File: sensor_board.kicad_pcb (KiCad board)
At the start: 2 copper layers, 96.5 x 64.8 mm, 13 parts, among them P1 CONN_01X06, P2 CONN_01X10

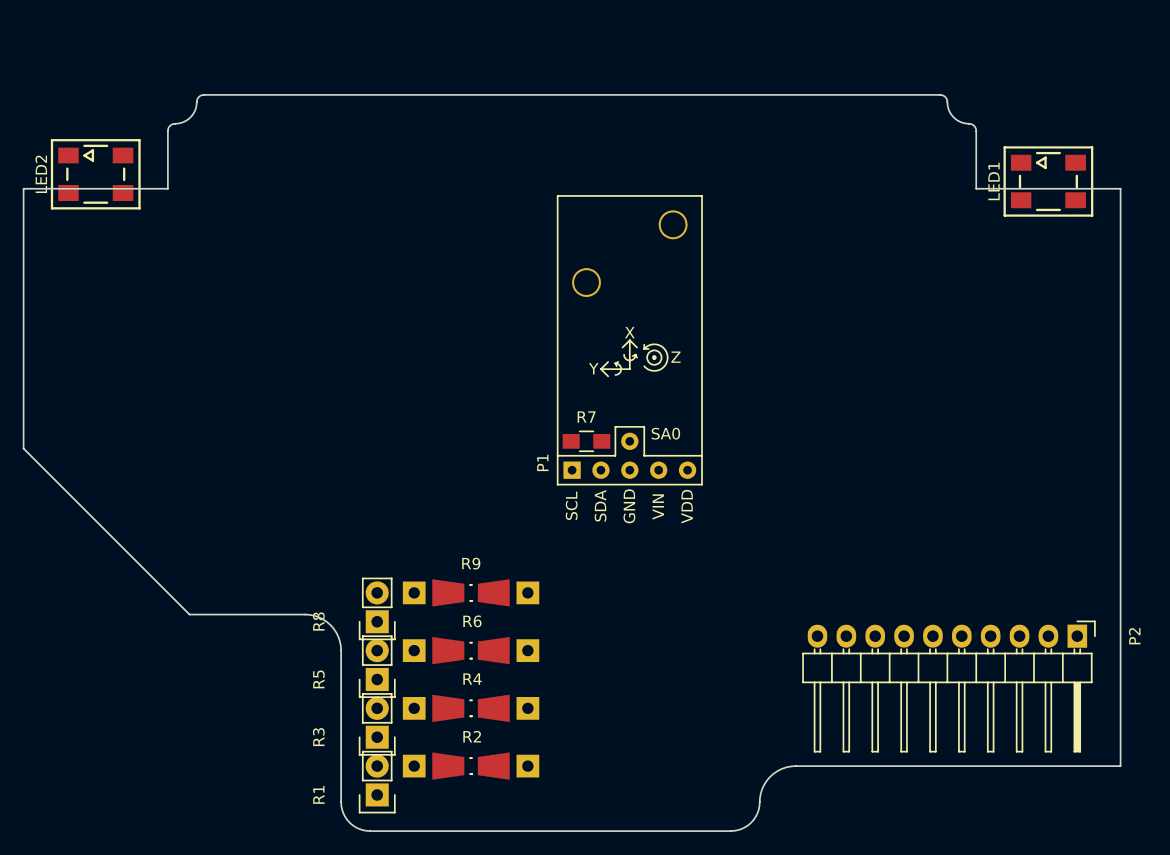
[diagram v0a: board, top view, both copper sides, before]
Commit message: Cleaned up schematics and sensor board PCB
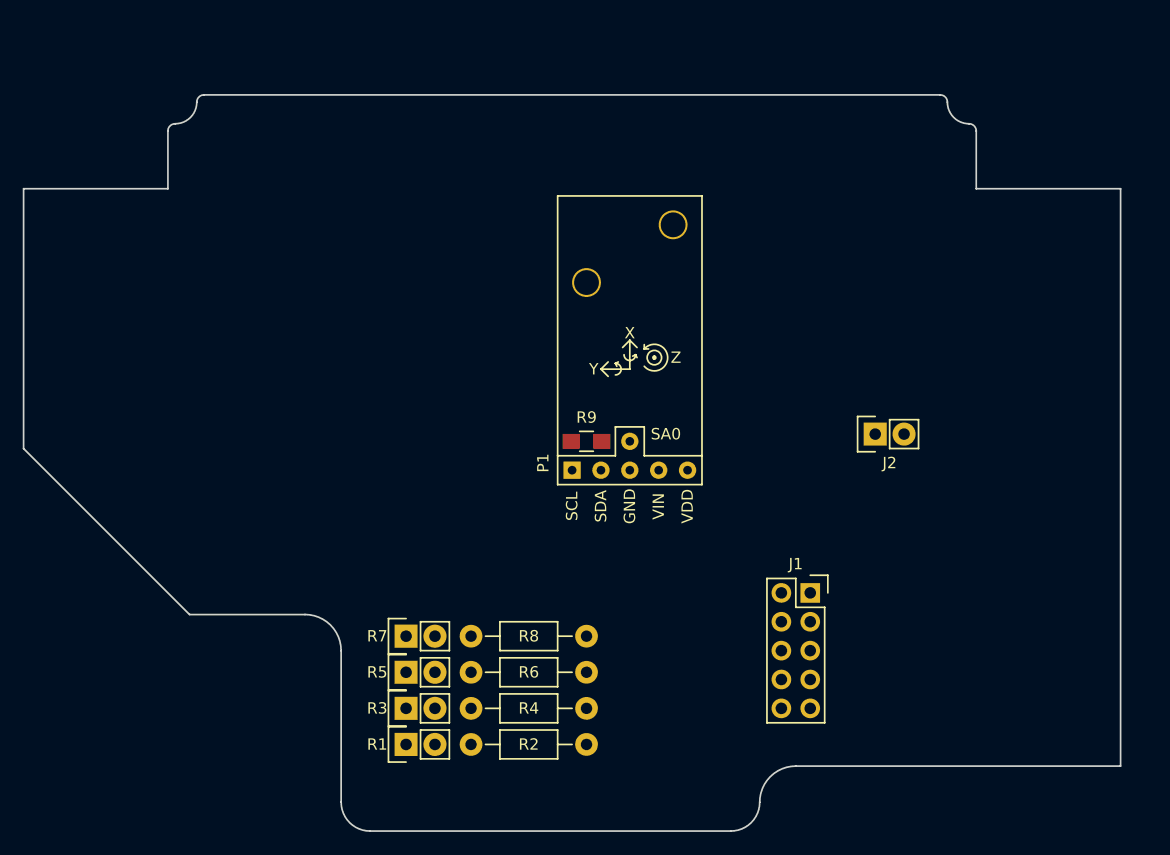
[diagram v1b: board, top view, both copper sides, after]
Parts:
- removed LED1, LED2: WS2812B, custom:PLCC4-5050
- removed P2: CONN_01X10, Pin_Headers:Pin_Header_Angled_1x10
- removed the R9 at (143.5, 123.8)
- added J1: HEADER_5x2, Socket_Strips:Socket_Strip_Straight_2x05, F.Cu at (173.4, 123.8)
- added J2: HEADER_2, Socket_Strips:Socket_Strip_Straight_1x02, F.Cu at (179.1, 109.9)
- added R8: 1M, Resistors_ThroughHole:Resistor_Horizontal_RM10mm, F.Cu at (143.5, 127.6)
- R2, R4, R6: value 100k -> 1M; footprint Resistors_Universal:Resistor_SMD+THTuniversal_0805to1206_RM10_HandSoldering_RevA_Date25Jun2010 -> Resistors_ThroughHole:Resistor_Horizontal_RM10mm
- moved R1 5.12 mm to (137.8, 137.2), turned to 0 degrees
- moved R3 3.59 mm to (137.8, 134.0), turned to 0 degrees
- moved R7 2.84 mm to (137.8, 127.6), turned to 0 degrees
- moved R5 2.62 mm to (137.8, 130.8), turned to 0 degrees
- moved R2 1.91 mm to (143.5, 137.2)
- moved R6 1.91 mm to (143.5, 130.8)
- renumbered R8 to R7, R7 to R9

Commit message: Sensor board revised fit within a 5cmX5cm square
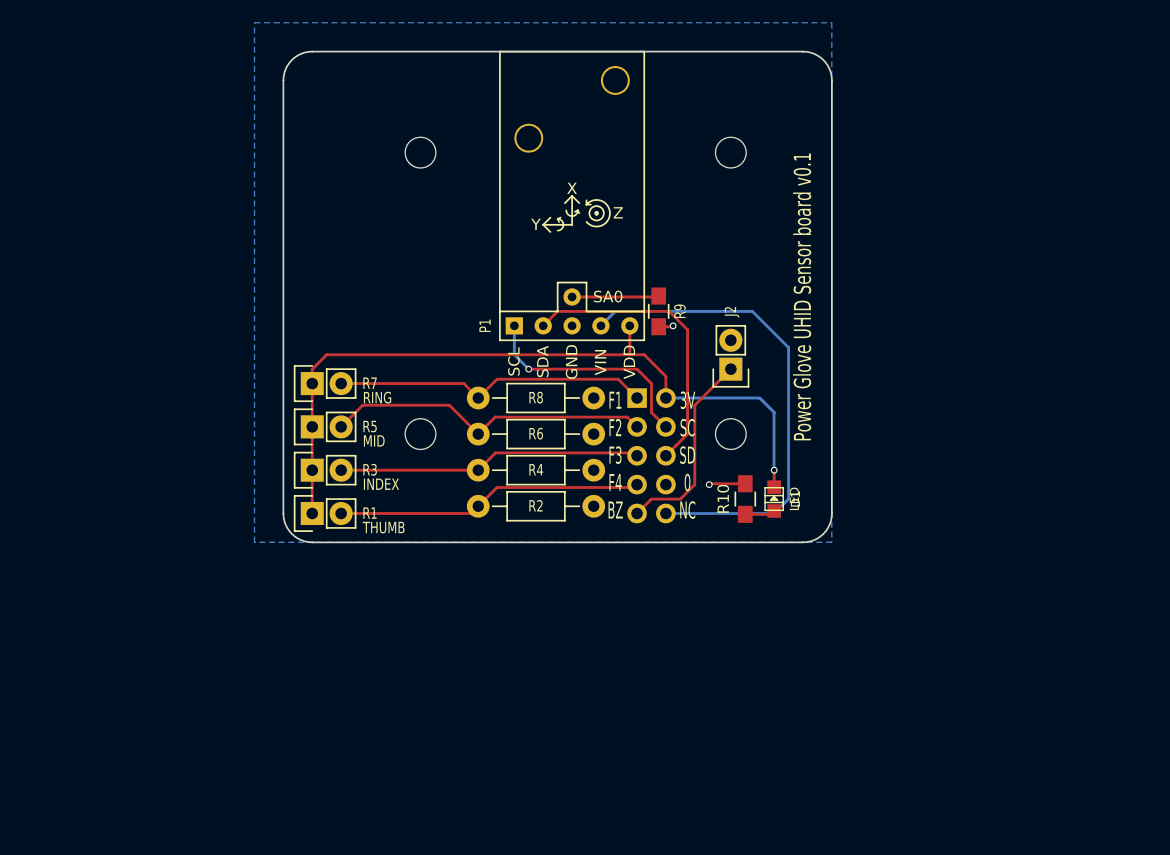
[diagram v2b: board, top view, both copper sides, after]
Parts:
- added D1: LED, w_smd_leds:Led_0805, F.Cu at (170.2, 115.6)
- added R10: 1k, Resistors_SMD:R_0805_HandSoldering, F.Cu at (167.6, 115.6)
- added REF**: MountingHole_2.7mm_M2.5, Mounting_Holes:MountingHole_2.7mm_M2.5, F.Cu at (139.1, 109.9)
- added REF**: MountingHole_2.7mm_M2.5, Mounting_Holes:MountingHole_2.7mm_M2.5, F.Cu at (166.4, 109.9)
- added REF**: MountingHole_2.7mm_M2.5, Mounting_Holes:MountingHole_2.7mm_M2.5, F.Cu at (166.4, 85.1)
- added REF**: MountingHole_2.7mm_M2.5, Mounting_Holes:MountingHole_2.7mm_M2.5, F.Cu at (139.1, 85.1)
- J1: moved to B.Cu
- moved R7 23.7 mm to (129.5, 105.4)
- moved R5 23.1 mm to (129.5, 109.2)
- moved J1 22.9 mm to (158.1, 106.7)
- moved R3 22.5 mm to (129.5, 113.0)
- moved R1 21.9 mm to (129.5, 116.8)
- moved R4 21.0 mm to (144.1, 113.0)
- moved R2 21.0 mm to (144.1, 116.2)
- moved R6 21.0 mm to (144.1, 109.9)
- moved R8 21.0 mm to (144.1, 106.7)
- moved J2 13.9 mm to (166.4, 104.1), turned to 90 degrees
- moved P1 13.7 mm to (152.4, 100.3)
- moved R9 13.1 mm to (160.0, 99.1), turned to 90 degrees
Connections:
- J1 pad 10: Net-(J1-Pad10) -> /VIN
- P1 pad 4: Net-(P1-Pad4) -> /VIN
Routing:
- net +3V3: track 0.00 -> 66.2 mm, vias 0 -> 1
- net /VIN: track 0.00 -> 43.0 mm
- net /FLEX_MIDDLE: track 0.00 -> 28.9 mm
- net /FLEX_RING: track 0.00 -> 27.9 mm
- net /FLEX_THUMB: track 0.00 -> 27.1 mm
- net /FLEX_INDEX: track 0.00 -> 26.8 mm
- net /IMU_SDA: track 0.00 -> 25.8 mm
- net /IMU_SCL: track 0.00 -> 20.0 mm, vias 0 -> 1
- net /BUZZER: track 0.00 -> 17.6 mm
- net Net-(P1-Pad6): track 0.00 -> 7.65 mm
- net GND: track 0.00 -> 4.51 mm, vias 0 -> 2
- net Net-(D1-Pad1): track 0.00 -> 2.66 mm
- added copper zone on B.Cu, net GND
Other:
- board size 96.5 x 64.8 mm -> 48.3 x 43.2 mm
- board text added: "3V SC SD 0 NC"
- board text added: "F1 F2 F3 F4 BZ"
- board text added: "INDEX"
- board text added: "MID"
- board text added: "Power Glove UHID Sensor board v0.1"
- board text added: "RING"
- board text added: "THUMB"

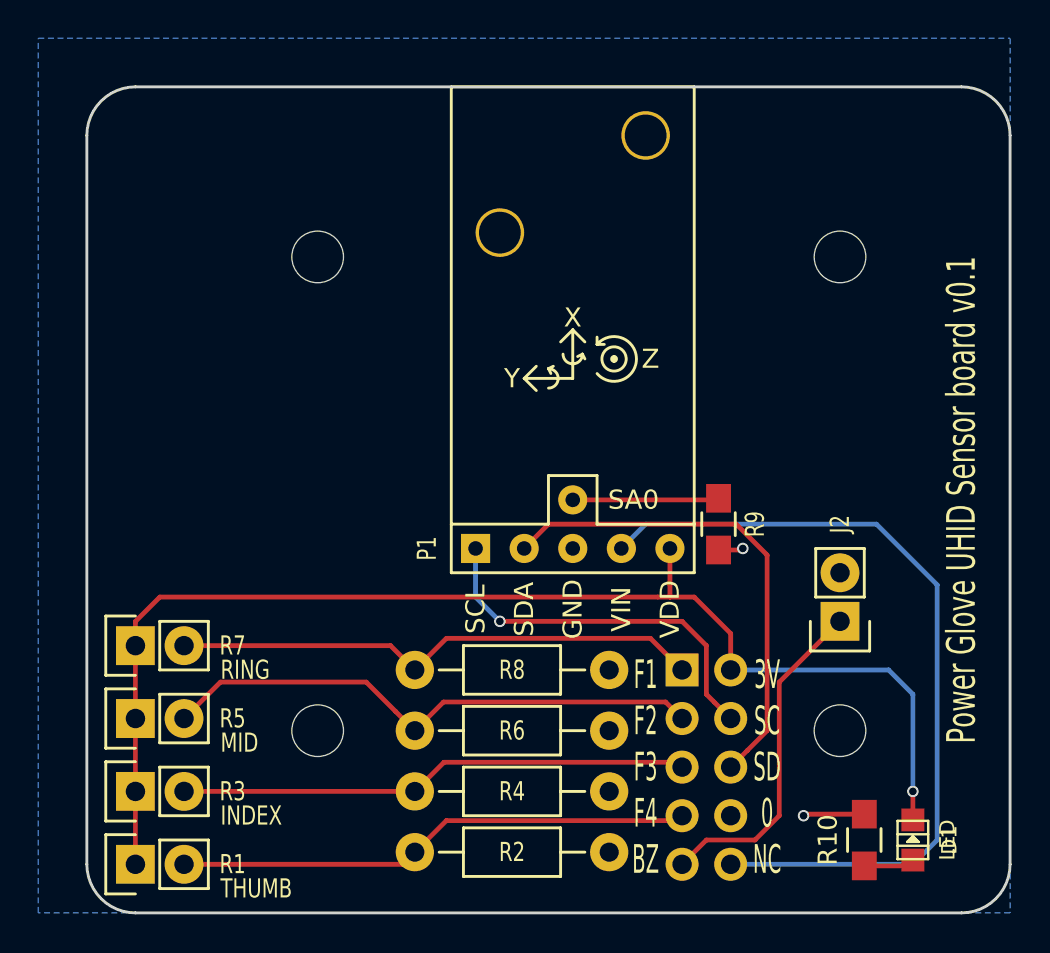
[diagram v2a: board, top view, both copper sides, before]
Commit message: Rearranged sensor board components for cleanliness
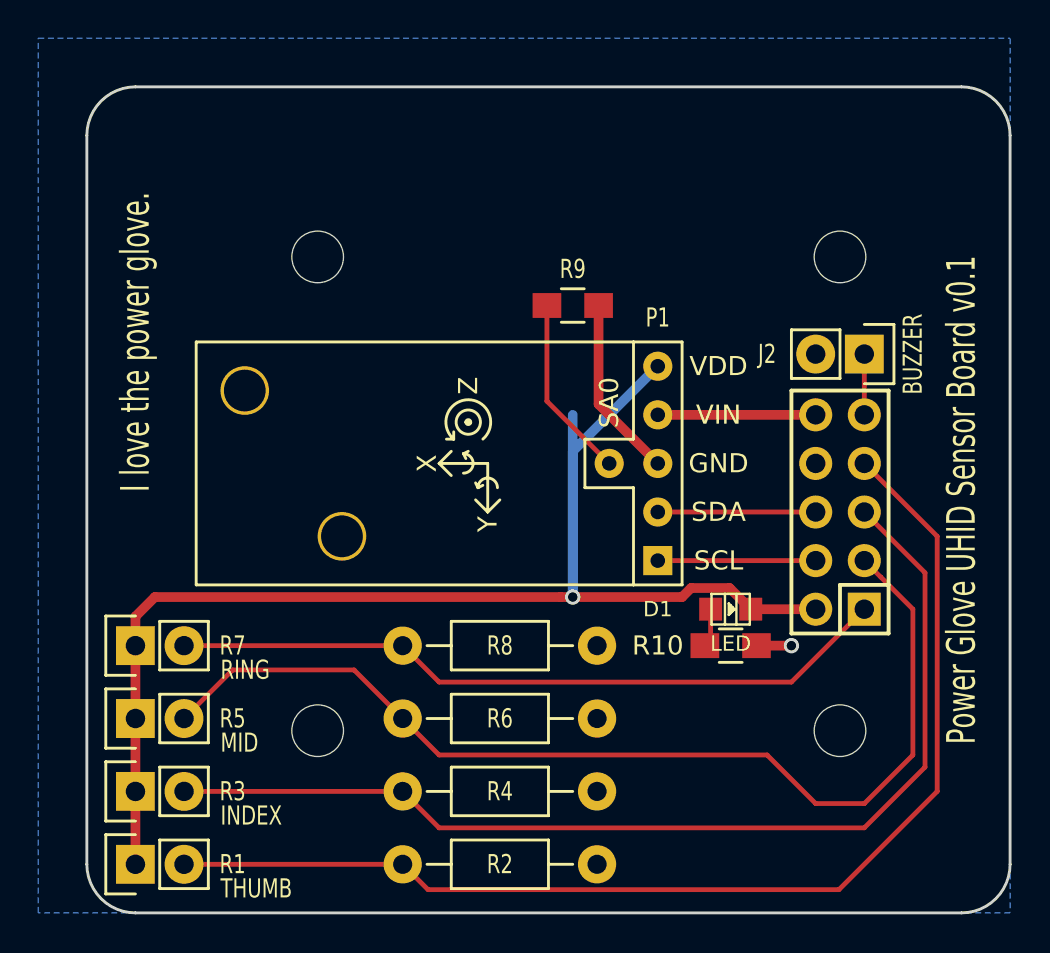
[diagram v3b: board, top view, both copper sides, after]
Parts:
- moved D1 15.4 mm to (160.7, 103.5), turned to 0 degrees
- moved J2 14.0 mm to (167.6, 90.2), turned to 180 degrees
- moved R9 13.7 mm to (152.4, 87.6), turned to 180 degrees
- moved R10 12.3 mm to (160.7, 105.4), turned to 180 degrees
- moved J1 10.0 mm to (167.6, 103.5), turned to 90 degrees
- moved P1 6.29 mm to (156.8, 95.9), turned to 90 degrees
- moved R8 1.42 mm to (143.5, 105.4)
- moved R2 0.90 mm to (143.5, 116.8)
- moved R6 0.90 mm to (143.5, 109.2)
- moved R4 0.64 mm to (143.5, 113.0)
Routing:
- net /VIN: track 43.0 -> 8.25 mm
- net /FLEX_THUMB: track 27.1 -> 60.8 mm
- net /FLEX_INDEX: track 26.8 -> 55.5 mm
- net /FLEX_MIDDLE: track 28.9 -> 54.3 mm
- net /IMU_SDA: track 25.8 -> 8.25 mm
- net /BUZZER: track 17.6 -> 3.17 mm
- net /IMU_SCL: track 20.0 -> 8.25 mm, vias 1 -> 0
- net /FLEX_RING: track 27.9 -> 37.9 mm
- net GND: track 4.51 -> 11.4 mm, vias 2 -> 1
- net +3V3: track 66.2 -> 73.0 mm
- net Net-(P1-Pad6): track 7.65 -> 9.60 mm
- net Net-(D1-Pad1): track 2.66 -> 2.03 mm
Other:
- net class Default: clearance 0.2 -> 0.254; trace_width 0.25 -> 0.254
- net class Power added: clearance 0.254, trace_width 0.508, via_dia 0.8, via_drill 0.5
- rule trace_clearance: 0.2 -> 0.254
- board text added: "BUZZER"
- board text added: "I love the power glove."
- board text added: "Power Glove UHID Sensor Board v0.1"
- board text removed: "3V SC SD 0 NC"
- board text removed: "F1 F2 F3 F4 BZ"
- board text removed: "Power Glove UHID Sensor board v0.1"

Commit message: Sensor board images added, gerbers plotted
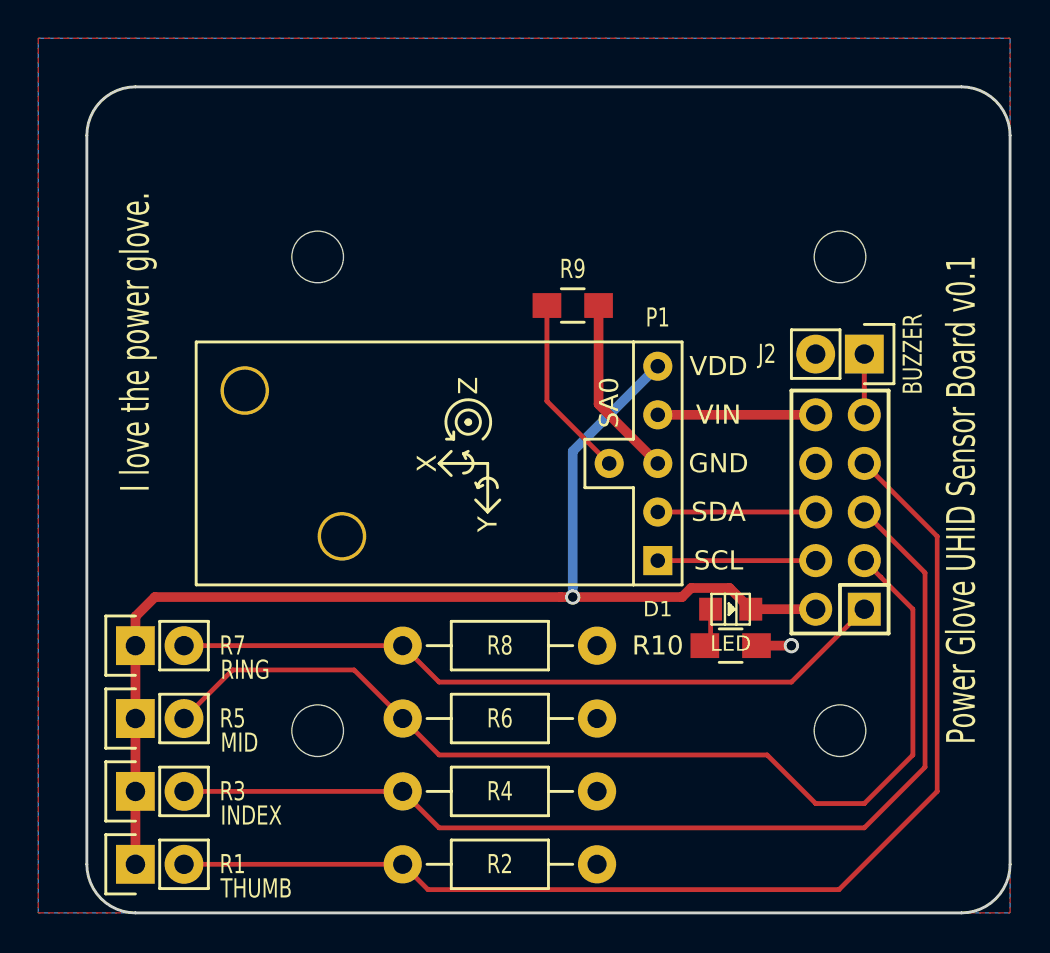
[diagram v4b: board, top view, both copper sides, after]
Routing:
- net +3V3: track 73.0 -> 63.5 mm
- added copper zone on F.Cu, net GND
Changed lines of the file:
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@@
     (thickness 1.6)
     (drawings 25)
-    (tracks 56)
+    (tracks 55)
     (zones 0)
     (modules 18)
@@
     (visible_elements 7FFEFFFF)
     (pcbplotparams
-      (layerselection 0x01000_00000000)
-      (usegerberextensions false)
+      (layerselection 0x010f0_80000001)
+      (usegerberextensions true)
       (excludeedgelayer true)
       (linewidth 0.200000)
@@
       (psa4output false)
       (plotreference true)
-      (plotvalue true)
+      (plotvalue false)
       (plotinvisibletext false)
       (padsonsilk false)
@@
       (drillshape 0)
       (scaleselection 1)
-      (outputdirectory ""))
+      (outputdirectory gerbers/sensor_board/))
   )
   (net 0 "")
@@
   (via (at 152.4 102.87) (size 0.8) (drill 0.5) (layers F.Cu B.Cu) (net 5))
   (segment (start 156.845 90.805) (end 152.4 95.25) (width 0.508) (layer B.Cu) (net 5))
-  (segment (start 152.4 93.345) (end 152.4 102.87) (width 0.508) (layer B.Cu) (net 5))
   (segment (start 152.4 95.25) (end 152.4 102.304315) (width 0.508) (layer B.Cu) (net 5))
   (segment (start 129.54 113.03) (end 129.54 116.84) (width 0.508) (layer F.Cu) (net 5))
@@
       )
     )
+  )
+  (zone (net 1) (net_name GND) (layer F.Cu) (hatch edge 0.508)
+    (connect_pads (clearance 0.254))
+    (min_thickness 0.254)
+    (fill yes (arc_segments 16) (thermal_gap 0.508) (thermal_bridge_width 0.508))
+    (polygon
+      (pts
+        (xy 175.26 73.66) (xy 124.46 73.66) (xy 124.46 119.38) (xy 175.26 119.38)
+      )
+    )
